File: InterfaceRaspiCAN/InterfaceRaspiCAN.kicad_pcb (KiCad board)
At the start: 2 copper layers, 65 x 56 mm, 43 parts, among them J1 Raspberry_Pi_2_3, J10 Conn_02x01, J11 Conn_02x01, J12 Conn_02x01, J13 Conn_01x02, J14 Conn_01x02, J15 Conn_01x02, J16 Conn_01x02, J17 Conn_01x02, J18 Conn_01x02, J19 Conn_01x02, J2 CAN1, J20 Conn_01x02, J3 CAN2, J4 I2C1_5, J5 I2C2_5, J6 I2C3_5, J7 I2C4_5, Q1 BSS138, Q2 BSS138, U1 MCP2517FD-xSL, U2 MCP2558FD-xSN, U3 PCF8575, U4 PESD1CAN, Y2 40MHz

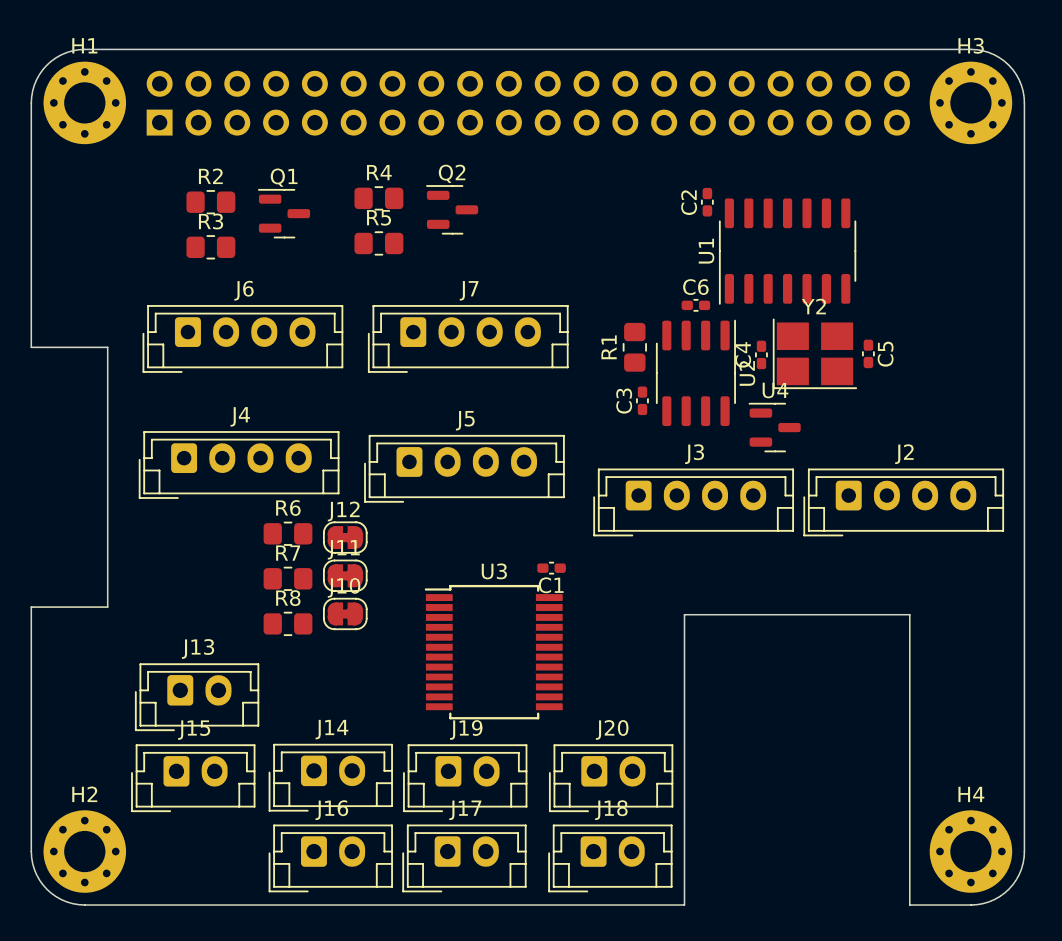
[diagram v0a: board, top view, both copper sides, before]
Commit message: Changes from discussion on meetings
- Remove 2x I2C connectors
- Remove 4x InApp programming connectors
- Change PCF8575 to PCF8574
- Change a half connectors to horizontal version
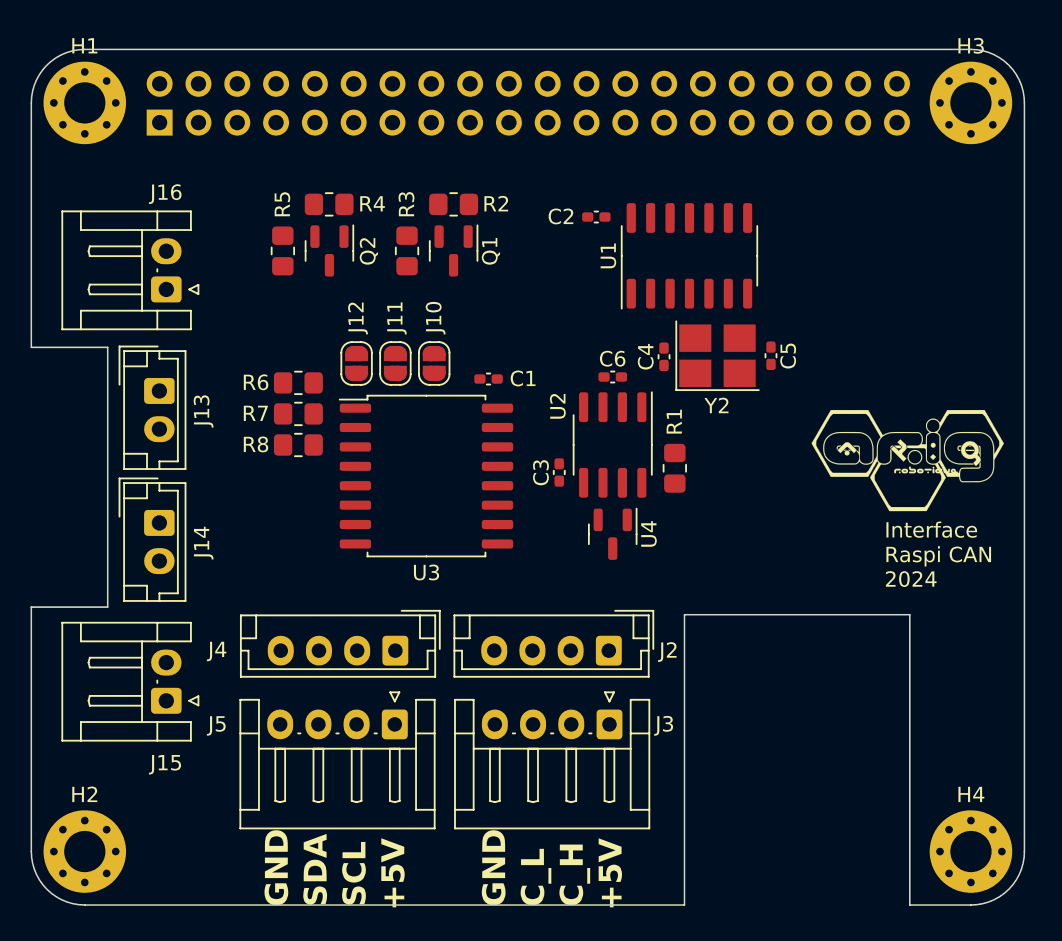
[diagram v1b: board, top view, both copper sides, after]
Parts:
- removed J17, J18, J19, J20: Conn_01x02, Connector_JST:JST_EH_B2B-EH-A_1x02_P2.50mm_Vertical
- removed J6: I2C3_5, Connector_JST:JST_EH_B4B-EH-A_1x04_P2.50mm_Vertical
- removed J7: I2C4_5, Connector_JST:JST_EH_B4B-EH-A_1x04_P2.50mm_Vertical
- added G***: LOGO, ARIG:Logo_ARIG_12_6x6_6, F.Cu at (133.9, 73.4)
- J10, J11, J12: footprint Jumper:SolderJumper-2_P1.3mm_Bridged_RoundedPad1.0x1.5mm -> Jumper:SolderJumper-2_P1.3mm_Open_RoundedPad1.0x1.5mm
- J15, J16: footprint Connector_JST:JST_EH_B2B-EH-A_1x02_P2.50mm_Vertical -> Connector_JST:JST_EH_S2B-EH_1x02_P2.50mm_Horizontal
- J3, J5: footprint Connector_JST:JST_EH_B4B-EH-A_1x04_P2.50mm_Vertical -> Connector_JST:JST_EH_S4B-EH_1x04_P2.50mm_Horizontal
- U3: value PCF8575 -> PCF8574A; footprint Package_SO:SSOP-24_5.3x8.2mm_P0.65mm -> Package_SO:SOIC-16W_7.5x10.3mm_P1.27mm
- moved J16 38.0 mm to (85.3, 62.2), turned to 90 degrees
- moved J13 19.6 mm to (84.9, 68.9), turned to -90 degrees
- moved J14 19.1 mm to (84.9, 77.5), turned to -90 degrees
- moved J4 18.7 mm to (100.3, 85.9), turned to 180 degrees
- moved J2 18.7 mm to (114.3, 85.9), turned to 180 degrees
- moved J10 17.4 mm to (102.9, 67.1), turned to -90 degrees
- moved J5 17.2 mm to (100.3, 90.7), turned to 180 degrees
- moved R2 15.9 mm to (104.1, 56.6), turned to 180 degrees
- moved J3 15.1 mm to (114.3, 90.7), turned to 180 degrees
- moved J11 14.3 mm to (100.3, 67.1), turned to -90 degrees
- moved C1 13.0 mm to (106.4, 68.1)
- moved R3 12.8 mm to (101.1, 59.7), turned to -90 degrees
- moved U4 12.7 mm to (114.6, 78.2), turned to -90 degrees
- moved U3 12.4 mm to (102.4, 74.4)
- moved R8 11.7 mm to (94.0, 72.4)
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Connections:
- U3 pad 1: unconnected-(U3-~{INT}-Pad1) -> Net-(J12-Pin_2)
- U3 pad 10: Net-(J16-Pin_1) -> Net-(J15-Pin_2)
- U3 pad 11: Net-(J16-Pin_2) -> Net-(J16-Pin_1)
- U3 pad 12: GND -> Net-(J16-Pin_2)
- U3 pad 13: Net-(J17-Pin_1) -> unconnected-(U3-~{INT}-Pad13)
- U3 pad 14: Net-(J17-Pin_2) -> SCL_5
- U3 pad 15: Net-(J18-Pin_1) -> SDA_5
- U3 pad 16: Net-(J18-Pin_2) -> +5VL
- U3 pad 8: Net-(J15-Pin_1) -> GND
- U3 pad 9: Net-(J15-Pin_2) -> Net-(J15-Pin_1)
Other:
- copper layers 2 -> 4
- board text added: "+5V"
- board text added: "C_H"
- board text added: "C_L"
- board text added: "GND"
- board text added: "Interface Raspi CAN 2024"
- board text added: "SCL"
- board text added: "SDA"

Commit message: Change inApp prog, CAN & I2C connectors
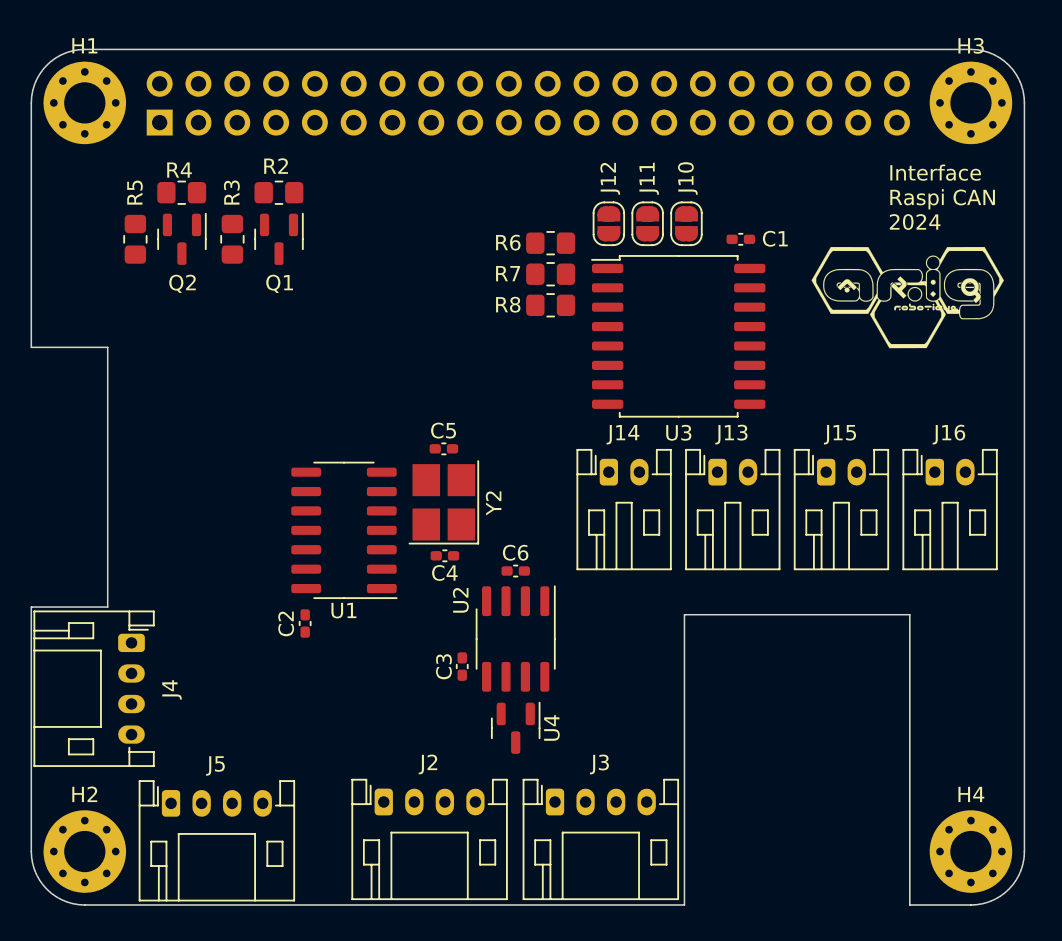
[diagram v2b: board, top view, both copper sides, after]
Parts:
- removed R1: 500, Resistor_SMD:R_0805_2012Metric_Pad1.20x1.40mm_HandSolder
- J13, J14: footprint Connector_JST:JST_EH_B2B-EH-A_1x02_P2.50mm_Vertical -> Connector_JST:JST_PH_S2B-PH-K_1x02_P2.00mm_Horizontal
- J15, J16: footprint Connector_JST:JST_EH_S2B-EH_1x02_P2.50mm_Horizontal -> Connector_JST:JST_PH_S2B-PH-K_1x02_P2.00mm_Horizontal
- J2, J4: footprint Connector_JST:JST_EH_B4B-EH-A_1x04_P2.50mm_Vertical -> Connector_JST:JST_PH_S4B-PH-K_1x04_P2.00mm_Horizontal
- J3, J5: footprint Connector_JST:JST_EH_S4B-EH_1x04_P2.50mm_Horizontal -> Connector_JST:JST_PH_S4B-PH-K_1x04_P2.00mm_Horizontal
- moved J16 51.7 mm to (135.6, 74.2), turned to 0 degrees
- moved J15 45.7 mm to (128.5, 74.2), turned to 0 degrees
- moved J13 36.9 mm to (121.4, 74.2), turned to 0 degrees
- moved C2 32.7 mm to (94.4, 84.1), turned to -90 degrees
- moved J14 29.6 mm to (114.3, 74.2), turned to 0 degrees
- moved U1 28.9 mm to (97.0, 78.0), turned to 180 degrees
- moved C5 22.3 mm to (103.5, 72.6), turned to 0 degrees
- moved Y2 20.3 mm to (103.5, 76.1), turned to 90 degrees
- moved C4 19.4 mm to (103.6, 79.6), turned to 180 degrees
- moved C1 18.9 mm to (122.9, 58.9)
- moved J11 18.9 mm to (116.8, 57.9)
- moved U3 18.9 mm to (118.9, 65.3)
- moved R7 18.9 mm to (110.5, 61.2)
- moved J10 18.9 mm to (119.4, 57.9)
- moved J12 18.9 mm to (114.3, 57.9)
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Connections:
- U2 pad 8: Net-(U2-S) -> GND
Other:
- board text removed: "+5V"
- board text removed: "C_H"
- board text removed: "C_L"
- board text removed: "GND"
- board text removed: "SCL"
- board text removed: "SDA"

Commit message: Fix CAN connections to improve routing on InterfaceRaspi
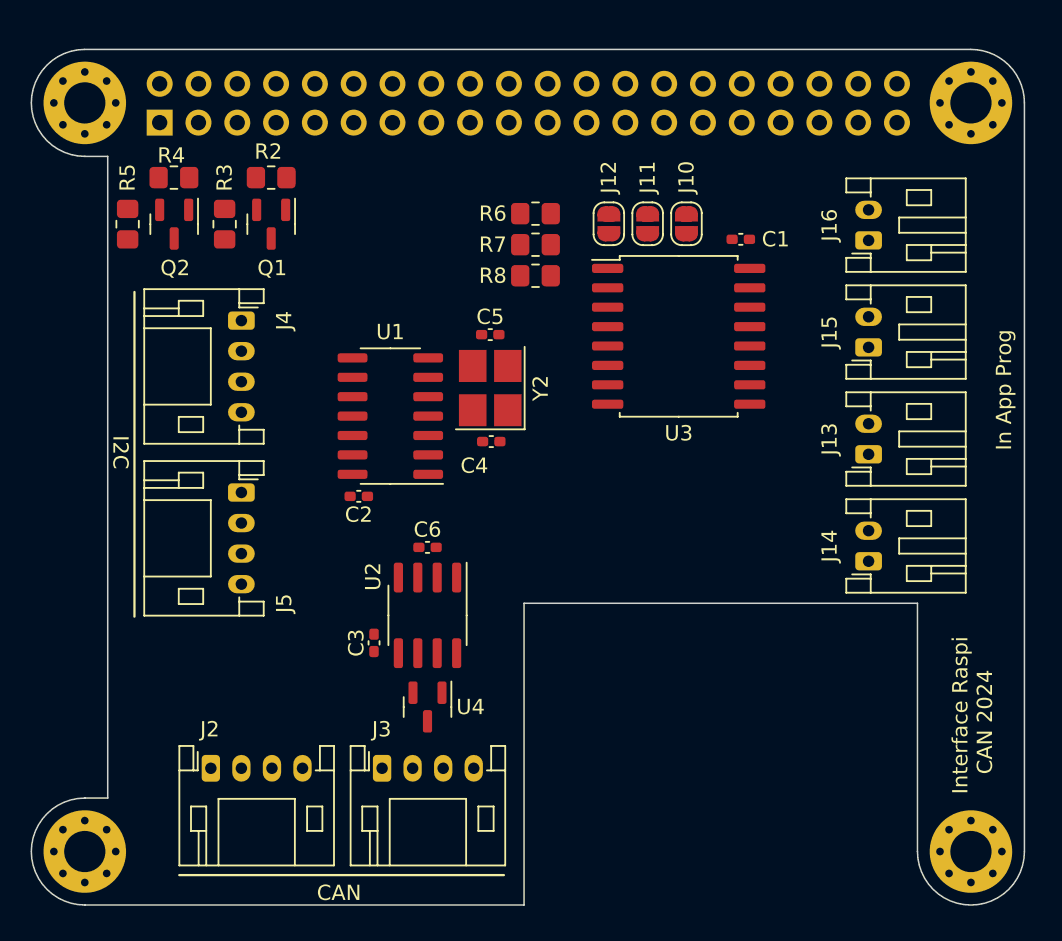
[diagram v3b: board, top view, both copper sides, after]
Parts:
- removed G***: LOGO, ARIG:Logo_ARIG_12_6x6_6
- moved J4 22.3 mm to (90.2, 64.2)
- moved J5 20.9 mm to (90.2, 75.5), turned to -90 degrees
- moved J14 18.0 mm to (131.3, 80.0), turned to 90 degrees
- moved J16 15.8 mm to (131.3, 59.0), turned to 90 degrees
- moved J2 11.5 mm to (88.2, 93.5)
- moved J3 11.5 mm to (99.5, 93.5)
- moved J13 9.96 mm to (131.3, 73.0), turned to 90 degrees
- moved C2 9.03 mm to (97.9, 75.8), turned to 0 degrees
- moved J15 8.63 mm to (131.3, 66.0), turned to 90 degrees
- moved C5 8.07 mm to (106.5, 65.2)
- moved Y2 8.07 mm to (106.5, 68.7)
- moved C4 8.07 mm to (106.6, 72.2)
- moved U1 8.07 mm to (100.0, 70.5)
- moved C3 5.98 mm to (98.9, 85.3)
- moved C6 5.98 mm to (102.4, 79.1)
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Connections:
- C1 pad 1: +5VL -> +3.3V
- J2 pad 2: CAN_H -> CAN_L
- J2 pad 3: CAN_L -> CAN_H
- J3 pad 2: CAN_H -> CAN_L
- J3 pad 3: CAN_L -> CAN_H
- R6 pad 1: +5VL -> +3.3V
- R7 pad 1: +5VL -> +3.3V
- R8 pad 1: +5VL -> +3.3V
- U3 pad 14: SCL_5 -> SCL33
- U3 pad 15: SDA_5 -> SDA_33
- U3 pad 16: +5VL -> +3.3V
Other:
- outline, holes or cut-outs redrawn
- board text added: "CAN"
- board text added: "I2C"
- board text added: "In App Prog"

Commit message: Upgrade to KiCad 8 and finish routing
- MasterAlimCAN
- InterfaceRaspiCAN
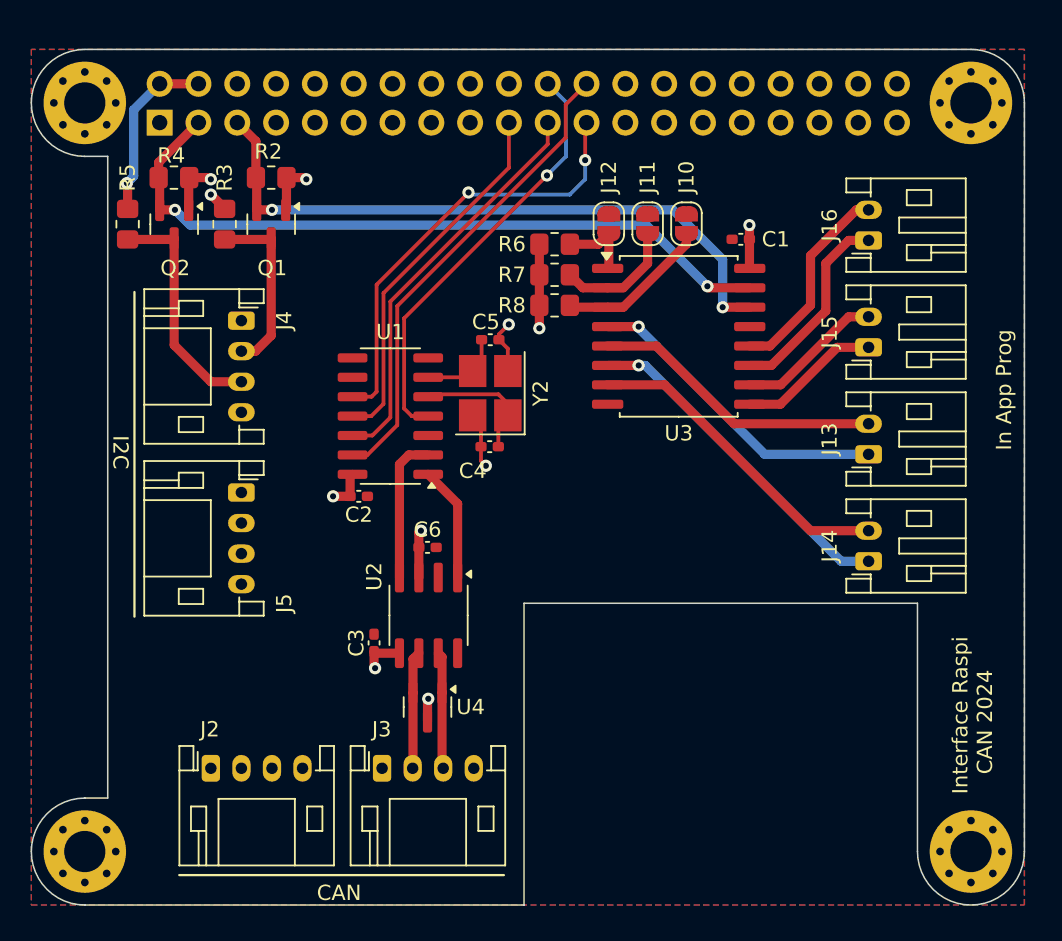
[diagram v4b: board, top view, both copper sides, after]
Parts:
- moved R6 2.36 mm to (110.8, 59.2)
- moved R7 2.33 mm to (110.8, 61.2)
- moved R8 2.30 mm to (110.8, 63.2)
- moved C4 0.35 mm to (106.5, 72.5)
- moved C5 0.33 mm to (106.5, 65.5)
- moved Y2 0.33 mm to (106.5, 69.0)
- moved U2 0.07 mm to (102.5, 83.5)
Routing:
- net SDA_33: track 0.00 -> 47.6 mm, vias 0 -> 2
- net SCL33: track 0.00 -> 43.0 mm, vias 0 -> 2
- net SPI_CS: track 0.00 -> 31.2 mm
- net SDA_5: track 0.00 -> 29.5 mm
- net SPI_CLK: track 0.00 -> 29.1 mm, vias 0 -> 2
- net CAN_INT: track 0.00 -> 27.9 mm, vias 0 -> 1
- net SPI_MISO: track 0.00 -> 26.5 mm
- net SCL_5: track 0.00 -> 26.0 mm
- net SPI_MOSI: track 0.00 -> 24.2 mm
- net Net-(J14-Pin_1): track 0.00 -> 22.4 mm, vias 0 -> 1
- net CAN_L: track 0.00 -> 21.6 mm
- net CAN_H: track 0.00 -> 21.5 mm
- net Net-(J14-Pin_2): track 0.00 -> 21.0 mm
- net +3.3V: track 0.00 -> 20.9 mm, vias 0 -> 6
- net Net-(J13-Pin_1): track 0.00 -> 20.6 mm, vias 0 -> 1
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- added copper zone on In2.Cu, net +3.3V
- added copper zone on In1.Cu, net +5VL
- added copper zone on B.Cu, net GND
- added copper zone on F.Cu, net GND

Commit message: Generate all production files
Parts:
- added G***: LOGO, ARIG:Logo_ARIG_12_6x6_6, F.Cu at (118.8, 75.5)
- C4, C5: value 15pF -> 12pF
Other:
- outline, holes or cut-outs redrawn
